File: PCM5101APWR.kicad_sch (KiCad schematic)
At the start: 1 part, among them U1 PCM5101A

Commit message: pushies
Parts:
- added C1, C2: C_Small, symbol Device:C_Small
- added J1, J2: AudioJack2, Connector_Audio:Jack_speakON-6.35mm_Neutrik_NLJ2MDXX-H_Horizontal, symbol Connector_Audio:AudioJack2
- added J3: Conn_01x06, symbol Connector_Generic:Conn_01x06
- added R1, R2, R3, R4: R_Small, symbol Device:R_Small
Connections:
- net GND: now also C1.2, C2.2, R3.1, R4.1
- net +3.3V: now reaches U1.1 (CPVDD)
- net +3.3V: now also U1.20 (DVDD), U1.8 (AVDD)
- net at U1.6 (OUTL): now also R1.1
- net at U1.7 (OUTR): now also R2.1
- new net: C1.1, J1.S, R2.2
- new net: J1.T, R4.2
- new net: J2.T, R3.2
- new net: C2.1, J2.S, R1.2
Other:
- note added: "Add LED to LRCK pin to as heartbeat for data transfer"

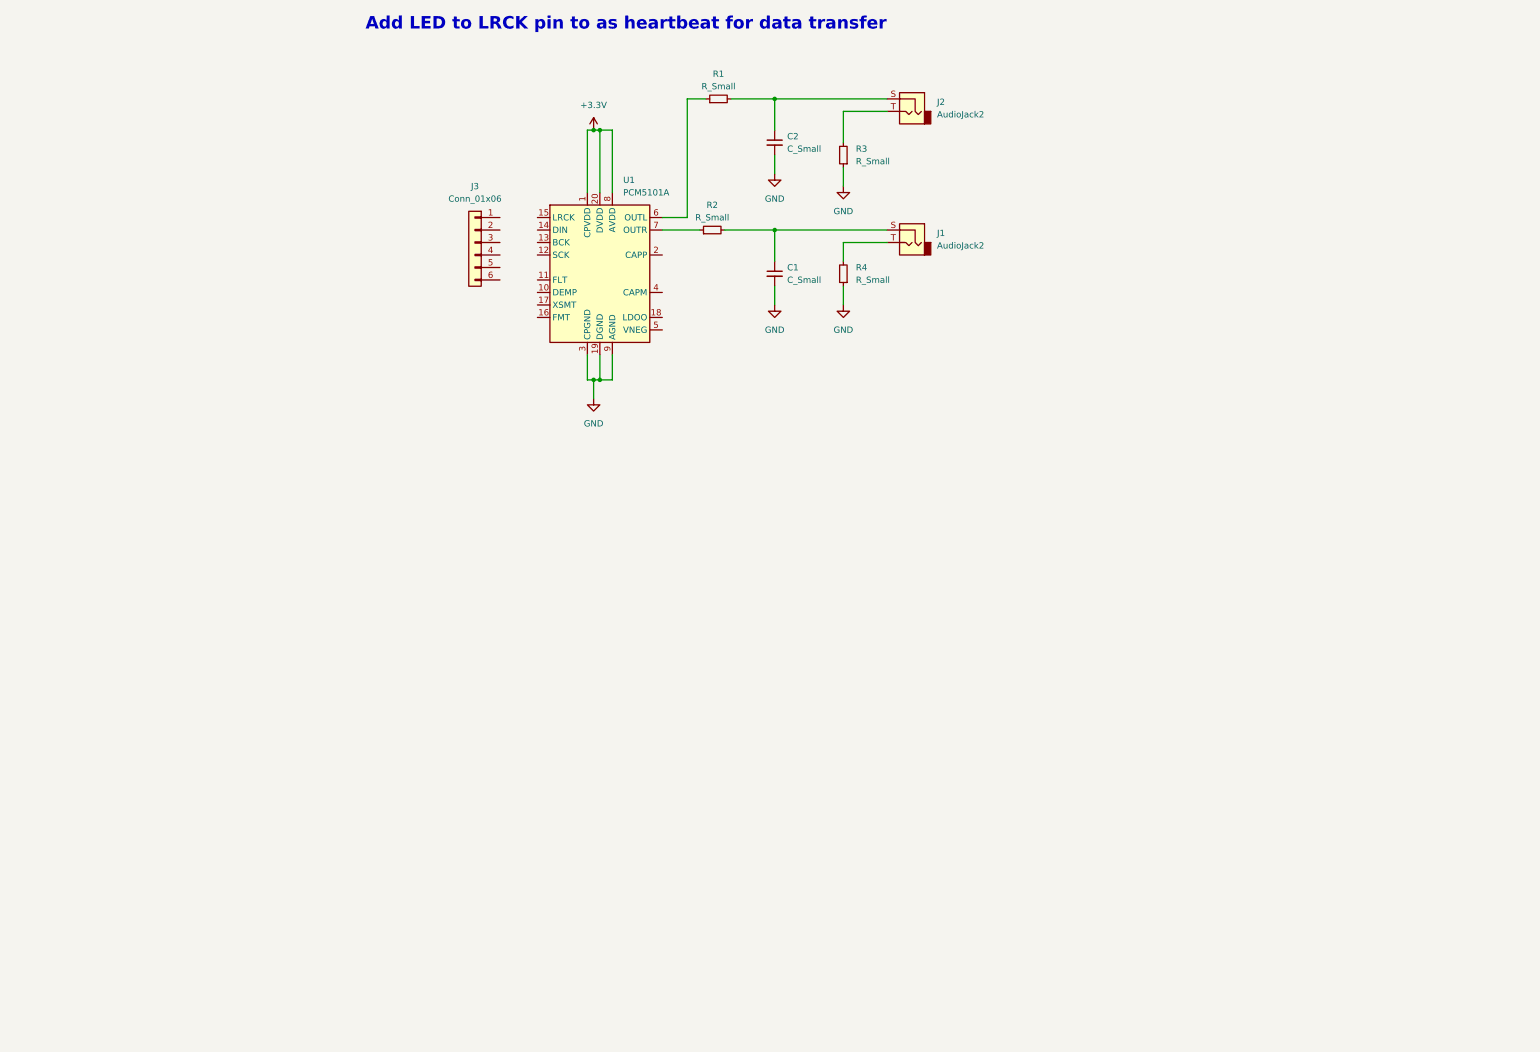
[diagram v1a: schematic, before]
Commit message: Added more connectors
Version change from 8 to 9
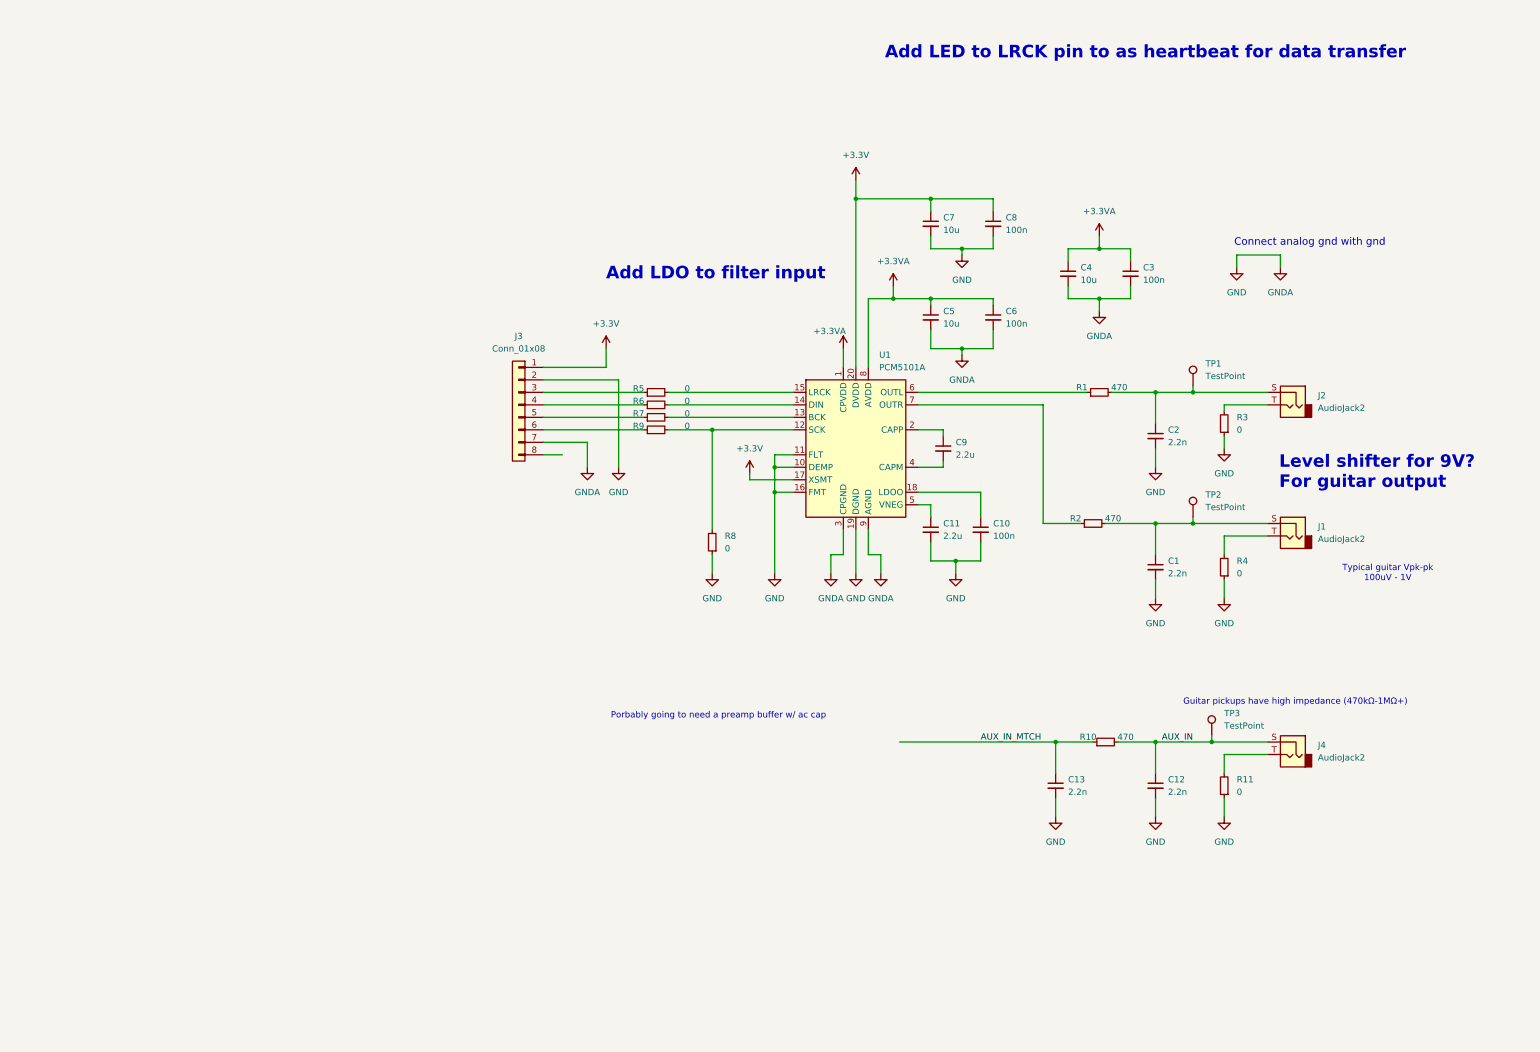
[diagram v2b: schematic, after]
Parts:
- removed J3: Conn_01x06, symbol Connector_Generic:Conn_01x06
- added C10, C3, C6, C8: 100n, Capacitor_SMD:C_0402_1005Metric, symbol Device:C_Small
- added C11, C9: 2.2u, Capacitor_SMD:C_0201_0603Metric, symbol Device:C_Small
- added C12, C13: 2.2n, Capacitor_SMD:C_0402_1005Metric, symbol Device:C_Small
- added C4, C5, C7: 10u, Capacitor_SMD:C_0201_0603Metric, symbol Device:C_Small
- added J3: Conn_01x08, symbol Connector_Generic:Conn_01x08
- added J4: AudioJack2, Connector_Audio:Jack_speakON-6.35mm_Neutrik_NLJ2MDXX-H_Horizontal, symbol Connector_Audio:AudioJack2
- added R10: 470, symbol Device:R_Small
- added R11, R5, R6, R7, R8, R9: 0, Resistor_SMD:R_0402_1005Metric, symbol Device:R_Small
- added TP1, TP2, TP3: TestPoint, TestPoint:TestPoint_Pad_D1.0mm, symbol Connector:TestPoint
- C1, C2: value C_Small -> 2.2n; footprint (none) -> Capacitor_SMD:C_0402_1005Metric
- R1, R2: value R_Small -> 470
- R3, R4: value R_Small -> 0; footprint (none) -> Resistor_SMD:R_0402_1005Metric
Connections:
- net +3.3V: now also U1.17 (XSMT), C7.1, C8.1, J3.1 (Pin_1); no longer U1.1 (CPVDD), U1.8 (AVDD)
- net GND: now also U1.10 (DEMP), U1.11 (FLT), U1.16 (FMT), C10.2, C11.2, C12.2, C13.2, C3.2, C4.2, C5.2, C6.2, C7.2, C8.2, J3.2 (Pin_2), J3.7 (Pin_7), R11.1, R8.1
- net at C1.1, J1.S, R2.2: now also TP2.1
- net at C2.1, J2.S, R1.2: now also TP1.1
- net at U1.12 (SCK): now also R8.2, R9.2
- net at U1.13 (BCK): now also R7.2
- net at U1.14 (DIN): now also R6.2
- net at U1.15 (LRCK): now also R5.2
- net at U1.18 (LDOO): now also C10.1
- net at U1.2 (CAPP): now also C9.1
- net at U1.4 (CAPM): now also C9.2
- net at U1.5 (VNEG): now also C11.1
- new net: J3.4 (Pin_4), R6.1
- new net: J3.3 (Pin_3), R5.1
- new net: J3.5 (Pin_5), R7.1
- new net: J3.6 (Pin_6), R9.1
- new net: J4.T, R11.2
- new net +3.3VA: C3.1, C4.1, C5.1, C6.1, U1.1 (CPVDD), U1.8 (AVDD)
- new net AUX_IN: C12.1, J4.S, R10.2, TP3.1
- new net AUX_IN_MTCH: C13.1, R10.1
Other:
- note added: "Add LDO to filter input"
- note added: "Connect analog gnd with gnd"
- note added: "Guitar pickups have high impedance (470kΩ-1MΩ+)"
- note added: "Level shifter for 9V? For guitar output"
- note added: "Porbably going to need a preamp buffer w/ ac cap"
- note added: "Typical guitar Vpk-pk 100uV - 1V"
- moved on the sheet: C1, C2, J1, J2, R1, R2, R3, R4, U1

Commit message: eco'ed to pcb
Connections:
- net AUX_IN_MTCH: now also J3.8 (Pin_8)
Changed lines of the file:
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@@
+	(wire
+		(pts
+			(xy 104.14 180.34) (xy 104.14 121.92)
+		)
+		(stroke
+			(width 0)
+			(type default)
+		)
+	)
 	(wire
 		(pts
@@
 	(wire
 		(pts
-			(xy 172.72 180.34) (xy 204.47 180.34)
-		)
-		(stroke
-			(width 0)
-			(type default)
-		)
-	)
-	(wire
-		(pts
 			(xy 147.32 129.54) (xy 147.32 146.05)
 		)
@@
 		)
 		(stroke
+			(width 0)
+			(type default)
+		)
+	)
+	(wire
+		(pts
+			(xy 104.14 180.34) (xy 204.47 180.34)
+		)
+		(stroke

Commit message: added buffer
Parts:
- added C14, C16: 100n, Capacitor_SMD:C_0402_1005Metric, symbol Device:C_Small
- added C15: 2.2u, Capacitor_SMD:C_0201_0603Metric, symbol Device:C_Small
- added R12, R13, R14, R15: 100k, Resistor_SMD:R_0402_1005Metric, symbol Device:R_Small
- added U2: MCP6002-xSN, symbol Amplifier_Operational:MCP6002-xSN
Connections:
- net +3.3VA: now also C16.2, R13.2, U2.8 (V+)
- net AUX_IN_MTCH: now also C14.2; no longer J3.8 (Pin_8)
- net GND: now also C15.2, C16.1, R12.1, U2.4 (V-)
- new net: R14.1, R15.2, U2.2 (-)
- new net: J3.8 (Pin_8), R14.2, U2.1
- new net: C15.1, R15.1
- new net: C14.1, R12.2, R13.1, U2.3 (+)

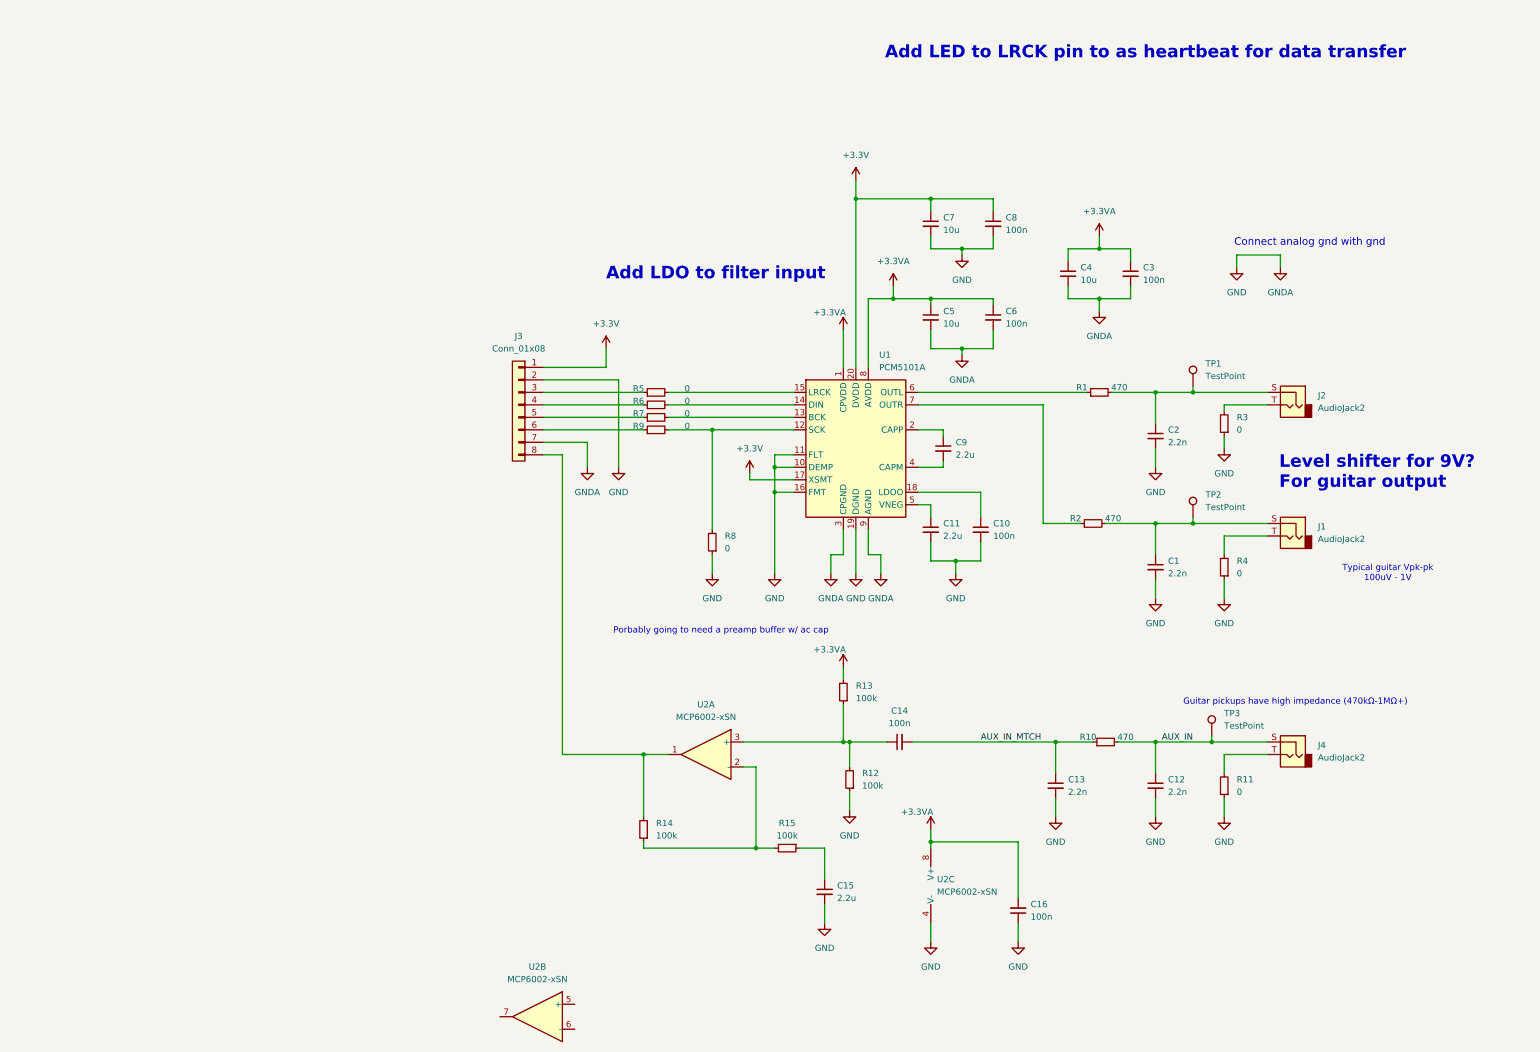
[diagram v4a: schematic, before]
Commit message: sch done. PCB started
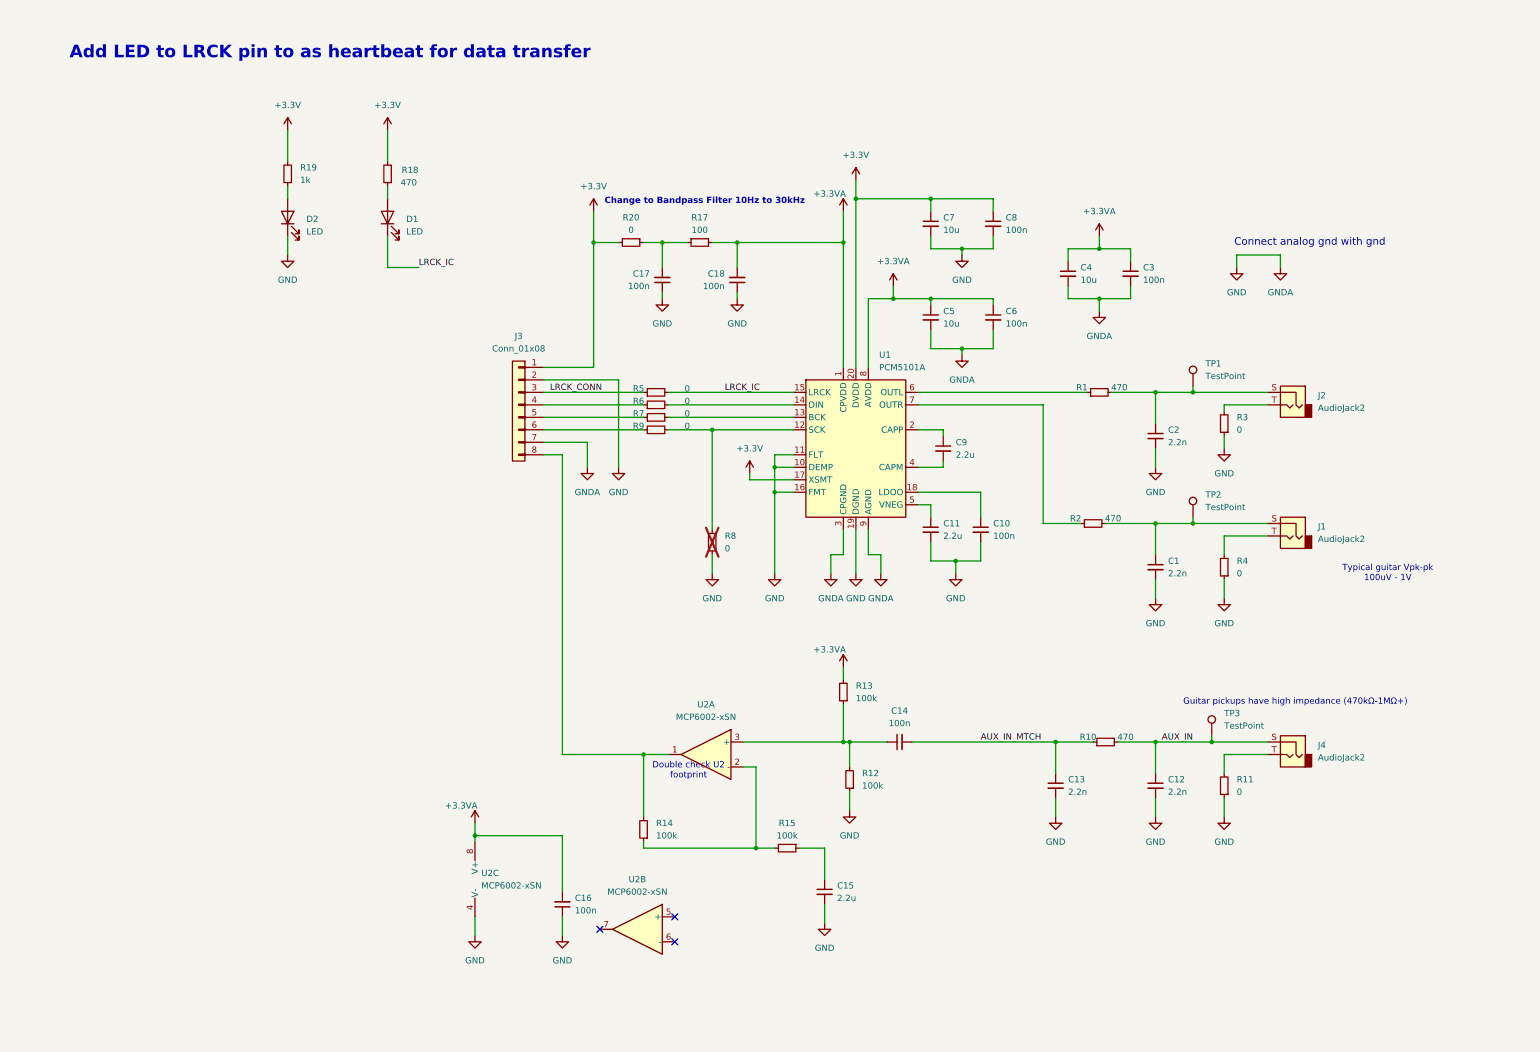
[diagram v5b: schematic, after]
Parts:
- added C17, C18: 100n, Capacitor_SMD:C_0603_1608Metric, symbol Device:C_Small
- added D1, D2: LED, LED_SMD:LED_0603_1608Metric, symbol Device:LED
- added R17: 100, Resistor_SMD:R_0603_1608Metric, symbol Device:R_Small
- added R18: 470, Resistor_SMD:R_0603_1608Metric, symbol Device:R_Small
- added R19: 1k, Resistor_SMD:R_0402_1005Metric, symbol Device:R_Small
- added R20: 0, Resistor_SMD:R_0603_1608Metric, symbol Device:R_Small
- C11, C15, C9: footprint Capacitor_SMD:C_0201_0603Metric -> Capacitor_SMD:C_0402_1005Metric
- C4, C5, C7: footprint Capacitor_SMD:C_0201_0603Metric -> Capacitor_SMD:C_0603_1608Metric
- J3: footprint (none) -> Connector_PinHeader_2.54mm:PinHeader_1x08_P2.54mm_Vertical
- R1, R10, R2: footprint (none) -> Resistor_SMD:R_0603_1608Metric
- R8: now not fitted
- U2: footprint (none) -> Package_SO:SOIC-8_5.3x5.3mm_P1.27mm
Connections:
- net +3.3V: now also R18.2, R19.2, R20.2
- net +3.3VA: now also C18.2, R17.2
- net GND: now also C17.1, C18.1, D2.1 (K)
- net LRCK_CONN: now reaches J3.3 (Pin_3), R5.1
- net LRCK_IC: now reaches R5.2, U1.15 (LRCK)
- net LRCK_IC: now also D1.1 (K)
- new net: D2.2 (A), R19.1
- new net: C17.2, R17.1, R20.1
- new net: D1.2 (A), R18.1
- no-connect marks 0 -> 3
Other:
- note added: "Change to Bandpass Filter 10Hz to 30kHz"
- note added: "Double check U2 footprint"
- note removed: "Add LDO to filter input"
- note removed: "Level shifter for 9V? For guitar output"
- note removed: "Porbably going to need a preamp buffer w/ ac cap"
- moved on the sheet: C16, U2B, U2C
